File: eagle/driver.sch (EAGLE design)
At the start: 4 parts

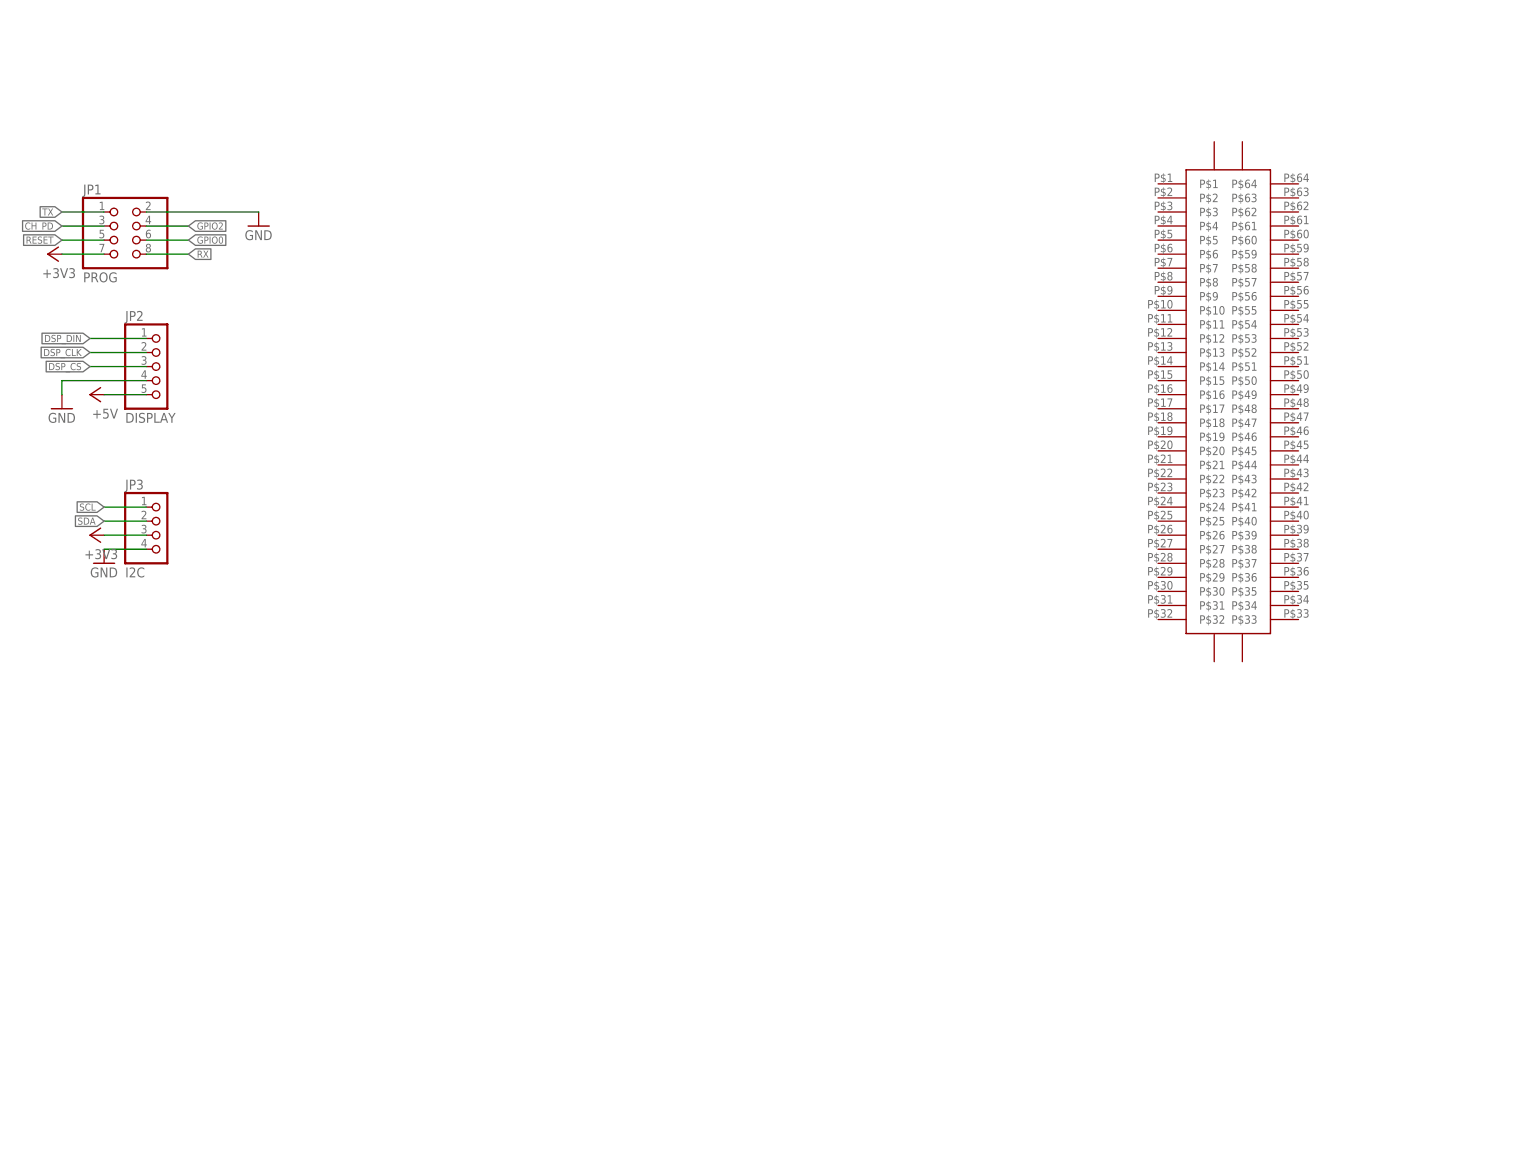
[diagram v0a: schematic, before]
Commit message: max7219 connection
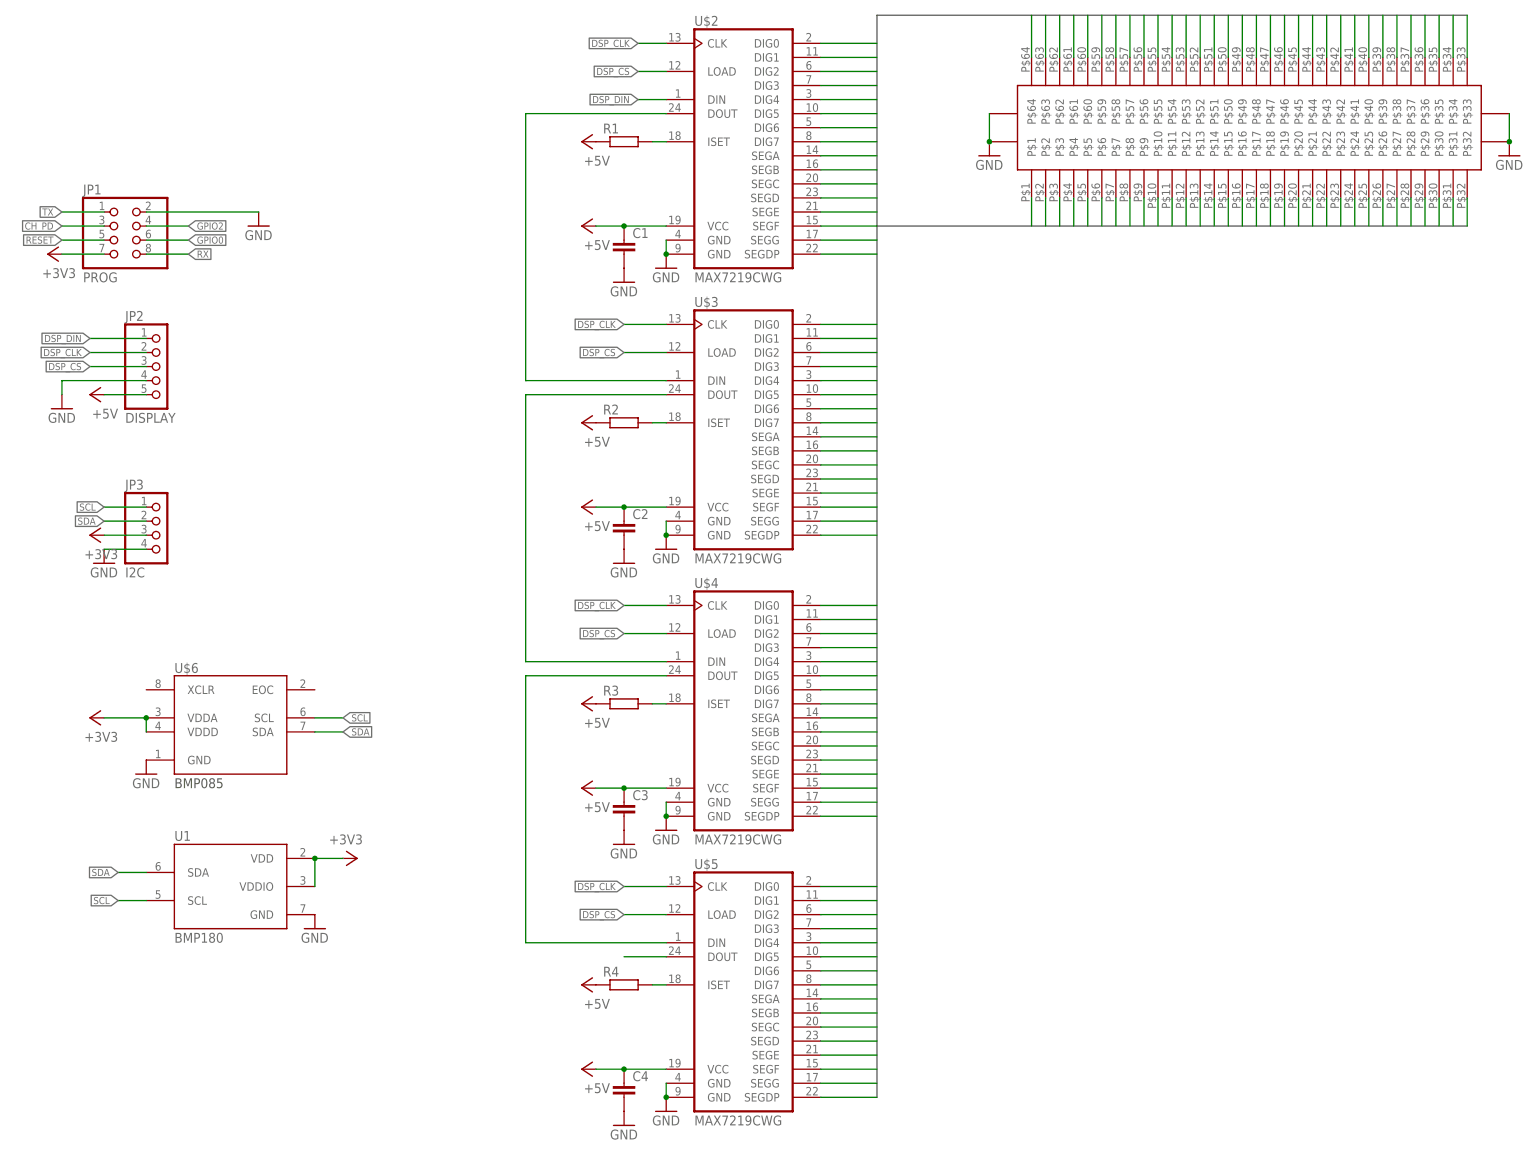
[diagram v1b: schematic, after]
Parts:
- added C1, C2, C3, C4: (no value), rcl:C-EUC0805
- added R1, R2, R3, R4: (no value), rcl:R-EU_R0805
- added U$2, U$3, U$4, U$5: MAX7219CWG, max7219:MAX7219CWG
- added U$6: BMP085, bmp085:BMP085
- added U1: BMP180, bmp180:BMP180
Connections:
- new net M1C1: U$1.P$64, U$2.DIG0
- new net M1C2: U$1.P$63, U$2.DIG1
- new net M1C3: U$1.P$62, U$2.DIG2
- new net M1C4: U$1.P$61, U$2.DIG3
- new net M1C5: U$1.P$60, U$2.DIG4
- new net M1C6: U$1.P$59, U$2.DIG5
- new net M1C7: U$1.P$58, U$2.DIG6
- new net M1C8: U$1.P$57, U$2.DIG7
- new net M1R1: U$1.P$1, U$2.SEGA
- new net M1R2: U$1.P$2, U$2.SEGB
- new net M1R3: U$1.P$3, U$2.SEGC
- new net M1R4: U$1.P$4, U$2.SEGD
- new net M1R5: U$1.P$5, U$2.SEGE
- new net M1R6: U$1.P$6, U$2.SEGF
- new net M1R7: U$1.P$7, U$2.SEGG
- new net M1R8: U$1.P$8, U$2.SEGDP
- new net M2C1: U$1.P$56, U$3.DIG0
- new net M2C2: U$1.P$55, U$3.DIG1
- new net M2C3: U$1.P$54, U$3.DIG2
- new net M2C4: U$1.P$53, U$3.DIG3
- new net M2C5: U$1.P$52, U$3.DIG4
- new net M2C6: U$1.P$51, U$3.DIG5
- new net M2C7: U$1.P$50, U$3.DIG6
- new net M2C8: U$1.P$49, U$3.DIG7
- new net M2R1: U$1.P$9, U$3.SEGA
- new net M2R2: U$1.P$10, U$3.SEGB
- new net M2R3: U$1.P$11, U$3.SEGC
- new net M2R4: U$1.P$12, U$3.SEGD
- new net M2R5: U$1.P$13, U$3.SEGE
- new net M2R6: U$1.P$14, U$3.SEGF
- new net M2R7: U$1.P$15, U$3.SEGG
- new net M2R8: U$1.P$16, U$3.SEGDP
- new net M3C1: U$1.P$48, U$4.DIG0
- new net M3C2: U$1.P$47, U$4.DIG1
- new net M3C3: U$1.P$46, U$4.DIG2
- new net M3C4: U$1.P$45, U$4.DIG3
- new net M3C5: U$1.P$44, U$4.DIG4
- new net M3C6: U$1.P$43, U$4.DIG5
- new net M3C7: U$1.P$42, U$4.DIG6
- new net M3C8: U$1.P$41, U$4.DIG7
- new net M3R1: U$1.P$17, U$4.SEGA
- new net M3R2: U$1.P$18, U$4.SEGB
- new net M3R3: U$1.P$19, U$4.SEGC
- new net M3R4: U$1.P$20, U$4.SEGD
- new net M3R5: U$1.P$21, U$4.SEGE
- new net M3R6: U$1.P$22, U$4.SEGF
- new net M3R7: U$1.P$23, U$4.SEGG
- new net M3R8: U$1.P$24, U$4.SEGDP
- new net M4C1: U$1.P$40, U$5.DIG0
- new net M4C2: U$1.P$39, U$5.DIG1
- new net M4C3: U$1.P$38, U$5.DIG2
- new net M4C4: U$1.P$37, U$5.DIG3
- new net M4C5: U$1.P$36, U$5.DIG4
- new net M4C6: U$1.P$35, U$5.DIG5
- new net M4C7: U$1.P$34, U$5.DIG6
- new net M4C8: U$1.P$33, U$5.DIG7
- new net M4R1: U$1.P$25, U$5.SEGA
- new net M4R2: U$1.P$26, U$5.SEGB
- new net M4R3: U$1.P$27, U$5.SEGC
- new net M4R4: U$1.P$28, U$5.SEGD
- new net M4R5: U$1.P$29, U$5.SEGE
- new net M4R6: U$1.P$30, U$5.SEGF
- new net M4R7: U$1.P$31, U$5.SEGG
- new net M4R8: U$1.P$32, U$5.SEGDP
- new net N$10: R2.2, U$3.ISET
- new net N$13: U$3.DOUT, U$4.DIN
- new net N$15: R3.2, U$4.ISET
- new net N$18: U$4.DOUT, U$5.DIN
- new net N$19: U$5.DOUT
- new net N$20: R4.2, U$5.ISET
- new net N$5: R1.2, U$2.ISET
- new net N$8: U$2.DOUT, U$3.DIN
- net +3V3: now also U$6.VDDA, U$6.VDDD, U1.VDD, U1.VDDIO
- net +5V: now also C1.1, C2.1, C3.1, C4.1, R1.1, R2.1, R3.1, R4.1, U$2.VCC, U$3.VCC, U$4.VCC, U$5.VCC
- net DSP_CLK: now also U$2.CLK, U$3.CLK, U$4.CLK, U$5.CLK
- net DSP_CS: now also U$2.LOAD, U$3.LOAD, U$4.LOAD, U$5.LOAD
- net DSP_DIN: now also U$2.DIN
- net GND: now also C1.2, C2.2, C3.2, C4.2, U$1.GND@1, U$1.GND@2, U$1.GND@3, U$1.GND@4, U$2.GND@1, U$2.GND@2, U$3.GND@1, U$3.GND@2, U$4.GND@1, U$4.GND@2, U$5.GND@1, U$5.GND@2, U$6.GND, U1.GND
- net SCL: now also U$6.SCL, U1.SCL
- net SDA: now also U$6.SDA, U1.SDA
